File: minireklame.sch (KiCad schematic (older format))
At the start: 34 parts, among them IC1 ATXMEGA64A4U-A, P1 CONN_01X02, P10 CONN_01X04, P11 CONN_01X04, P12 CONN_01X04, P13 CONN_01X04, P14 CONN_01X04, P15 CONN_01X04, P16 CONN_01X04, P17 CONN_01X04, P2 CONN_01X04, P3 CONN_01X02, P3 CONN_01X04, P4 CONN_01X04, P5 CONN_01X04, P6 CONN_01X04, P7 CONN_01X04, P8 CONN_01X04, P9 CONN_01X04, U1 TLV1117-33CDCYR, U2 SP3483-EN-L, U3 TLC5955

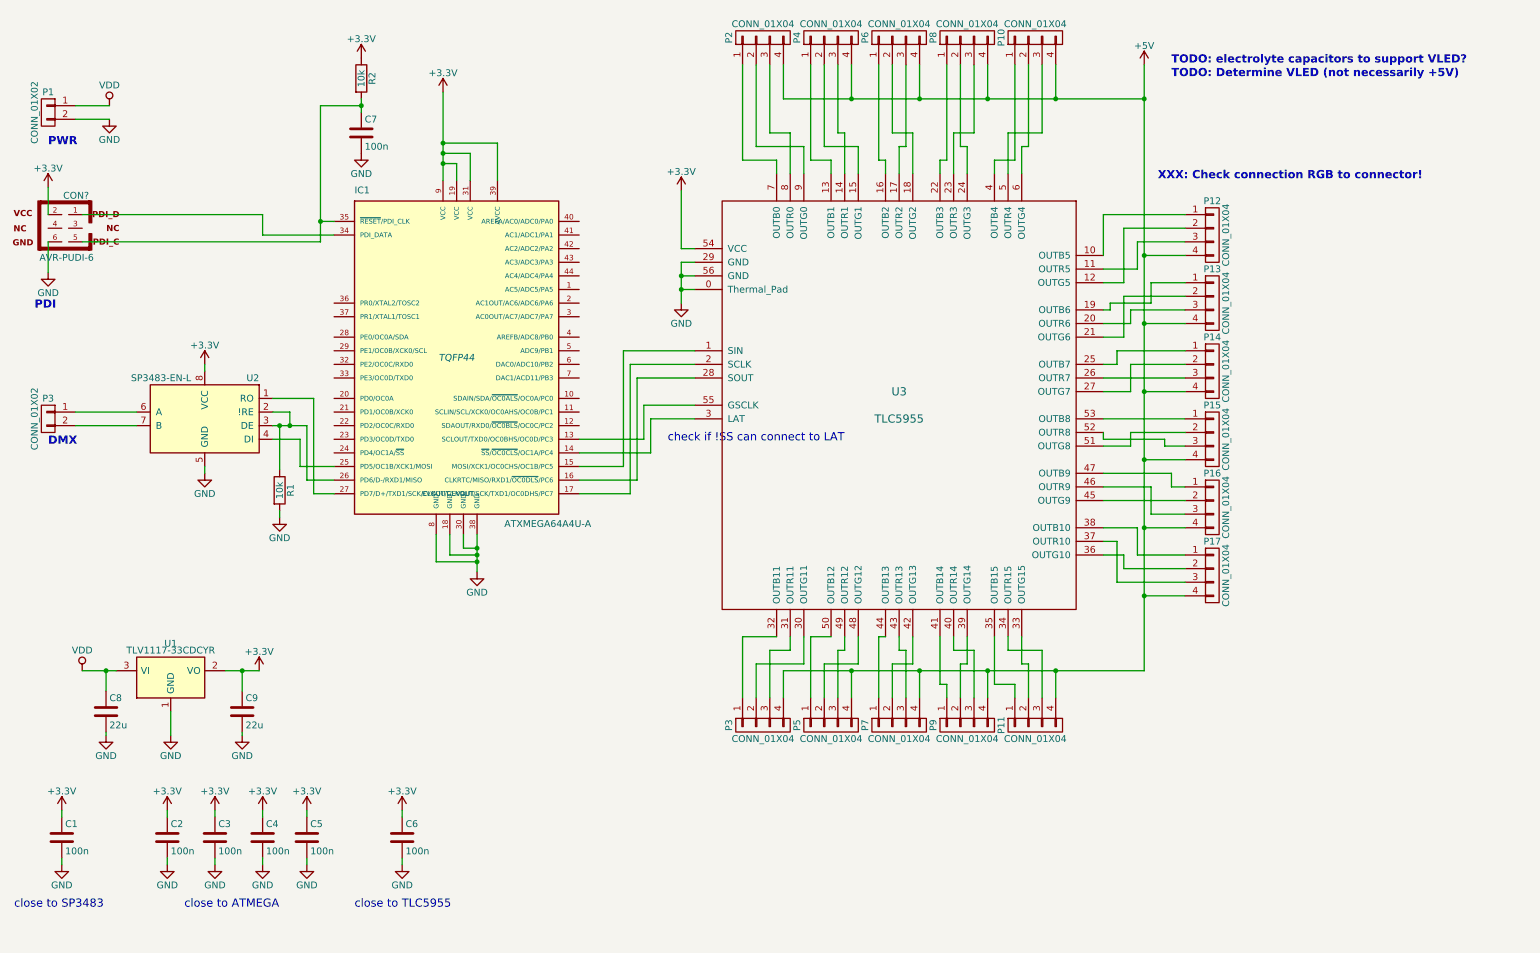
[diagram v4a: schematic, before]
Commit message: added optional XTAL
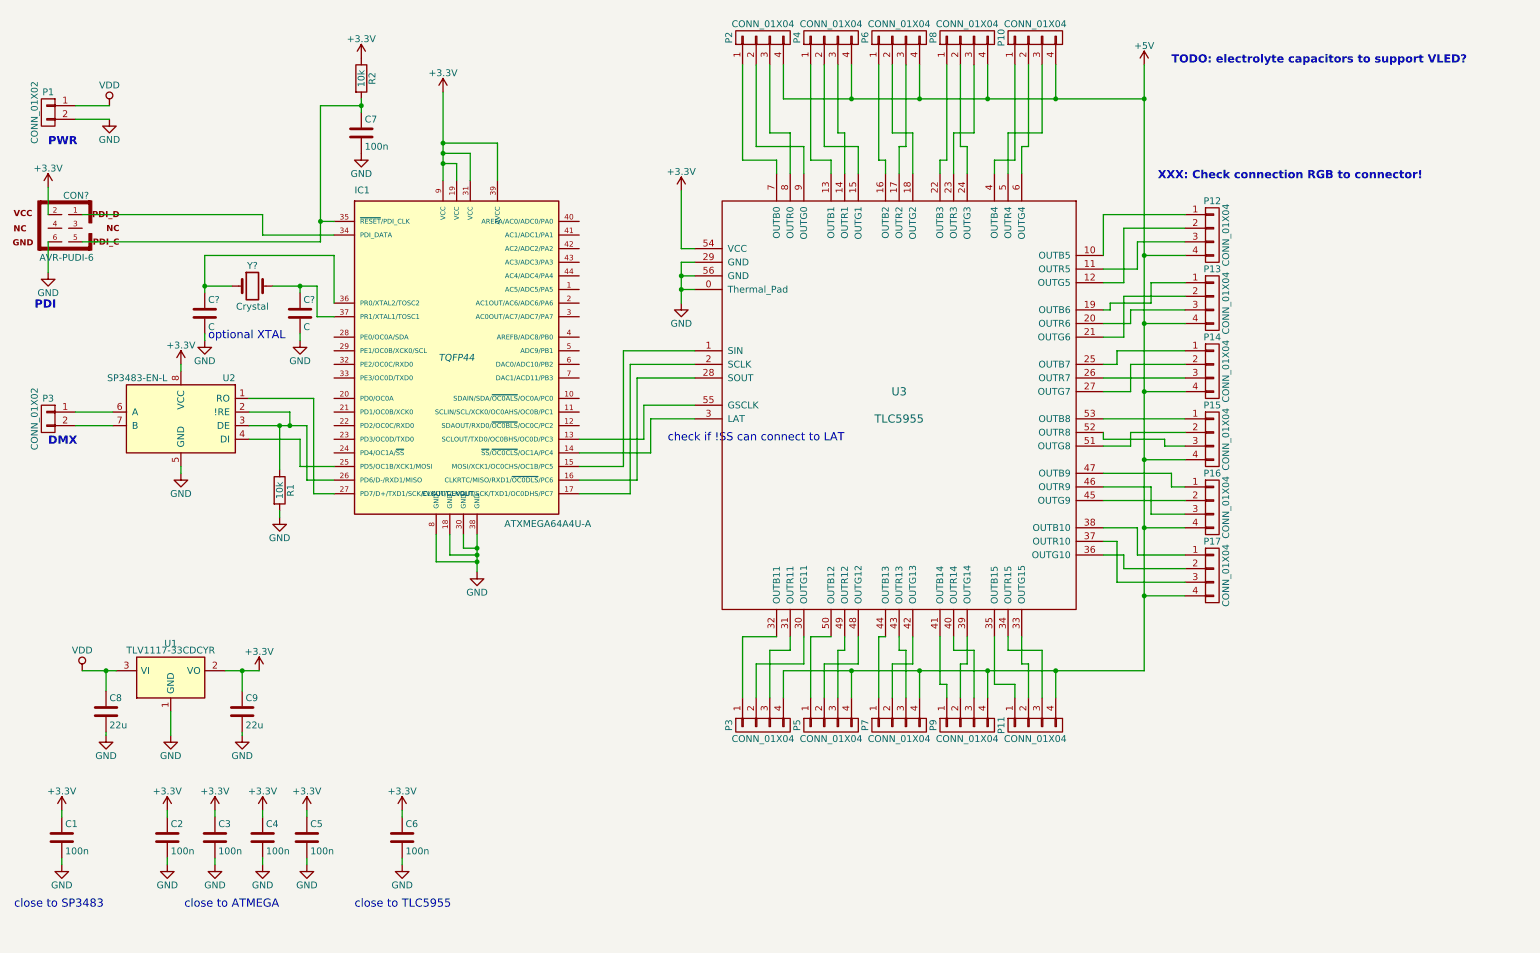
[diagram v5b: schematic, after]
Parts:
- added C? (x2): C, symbol C
- added Y?: Crystal, symbol Crystal
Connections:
- net GND: now also C?.2, C?.2
- net at IC1.36 (PR0/XTAL2/TOSC2): now also C?.1, Y?.1
- net at IC1.37 (PR1/XTAL1/TOSC1): now also C?.1, Y?.2
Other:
- note added: "optional XTAL"
- note removed: "TODO: Determine VLED (not necessarily +5V)"
- moved on the sheet: U2
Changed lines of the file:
@@
 L GND #PWR01
 U 1 1 58CAFE40
-P 2000 4150
-F 0 "#PWR01" H 2000 3900 50  0001 C CNN
-F 1 "GND" H 2000 4000 50  0000 C CNN
-F 2 "" H 2000 4150 50  0000 C CNN
-F 3 "" H 2000 4150 50  0000 C CNN
-	1    2000 4150
+P 1825 4150
+F 0 "#PWR01" H 1825 3900 50  0001 C CNN
+F 1 "GND" H 1825 4000 50  0000 C CNN
+F 2 "" H 1825 4150 50  0000 C CNN
+F 3 "" H 1825 4150 50  0000 C CNN
+	1    1825 4150
 	1    0    0    -1
 $EndComp
@@
 L SP3483-EN-L U2
 U 1 1 58CB0289
-P 2000 3750
-F 0 "U2" H 1600 4050 50  0000 L CNN
-F 1 "SP3483-EN-L" H 2100 4050 50  0000 L CNN
-F 2 "Housings_SOIC:SOIC-8_3.9x4.9mm_Pitch1.27mm" H 2000 3250 50  0001 C CIN
-F 3 "" H 2000 3750 50  0000 C CNN
-F 4 "SP3483EN-L" H 2000 3750 60  0001 C CNN "manf#"
-	1    2000 3750
+P 1825 3750
+F 0 "U2" H 1425 4050 50  0000 L CNN
+F 1 "SP3483-EN-L" H 1925 4050 50  0000 L CNN
+F 2 "Housings_SOIC:SOIC-8_3.9x4.9mm_Pitch1.27mm" H 1825 3250 50  0001 C CIN
+F 3 "" H 1825 3750 50  0000 C CNN
+F 4 "SP3483EN-L" H 1825 3750 60  0001 C CNN "manf#"
+	1    1825 3750
 	-1   0    0    -1
 $EndComp
@@
 L +3.3V #PWR02
 U 1 1 58CC36D0
-P 2000 3350
-F 0 "#PWR02" H 2000 3200 50  0001 C CNN
-F 1 "+3.3V" H 2000 3490 50  0000 C CNN
-F 2 "" H 2000 3350 50  0000 C CNN
-F 3 "" H 2000 3350 50  0000 C CNN
-	1    2000 3350
+P 1825 3350
+F 0 "#PWR02" H 1825 3200 50  0001 C CNN
+F 1 "+3.3V" H 1825 3490 50  0000 C CNN
+F 2 "" H 1825 3350 50  0000 C CNN
+F 3 "" H 1825 3350 50  0000 C CNN
+	1    1825 3350
 	1    0    0    -1
 $EndComp
@@
 $EndComp
 Wire Wire Line
-	1050 3700 1500 3700
-Wire Wire Line
-	1050 3800 1500 3800
-Wire Wire Line
-	2000 3350 2000 3400
+	1050 3700 1325 3700
+Wire Wire Line
+	1050 3800 1325 3800
+Wire Wire Line
+	1825 3350 1825 3400
 Wire Wire Line
 	3700 4600 3700 4800
@@
 	5500 2075 5500 2500
 Wire Wire Line
-	2500 3900 2700 3900
+	2325 3900 2700 3900
 Wire Wire Line
 	2700 3900 2700 4100
@@
 	2700 4100 2950 4100
 Wire Wire Line
-	2500 3800 2550 3800
+	2325 3800 2550 3800
 Wire Wire Line
 	2550 3800 2625 3800
@@
 	2750 4200 2950 4200
 Wire Wire Line
-	2500 3700 2625 3700
+	2325 3700 2625 3700
 Wire Wire Line
 	2625 3700 2625 3800
 Connection ~ 2625 3800
 Wire Wire Line
-	2500 3600 2800 3600
+	2325 3600 2800 3600
 Wire Wire Line
 	2800 3600 2800 4300
@@
 	1    0    0    -1
 $EndComp
-Text Notes 9100 1250 0    60   ~ 12
-TODO: Determine VLED (not necessarily +5V)
 $Comp
 L R R2
@@
 close to SP3483
 Wire Wire Line
-	2000 4150 2000 4100
+	1825 4150 1825 4100
 $Comp
 L +3.3V #PWR?
@@
 Text Notes 5400 3925 0    60   ~ 0
 check if !SS can connect to LAT
+$Comp
+L Crystal Y?
+U 1 1 591A9CF0
+P 2350 2775
+F 0 "Y?" H 2350 2925 50  0000 C CNN
+F 1 "Crystal" H 2350 2625 50  0000 C CNN
+F 2 "" H 2350 2775 50  0001 C CNN
+F 3 "" H 2350 2775 50  0001 C CNN
+	1    2350 2775
+	1    0    0    -1
+$EndComp
+Wire Wire Line
+	2950 2900 2950 2550
+Wire Wire Line
+	2950 2550 2000 2550
+Wire Wire Line
+	2000 2550 2000 2775
+Wire Wire Line
+	2000 2775 2000 2825
+Wire Wire Line
+	2000 2775 2200 2775
+Wire Wire Line
+	2950 3000 2825 3000
+Wire Wire Line
+	2825 3000 2825 2775
+Wire Wire Line
+	2825 2775 2700 2775
+Wire Wire Line
+	2700 2775 2500 2775
+$Comp
+L C C?
+U 1 1 591AA01D
+P 2000 2975
+F 0 "C?" H 2025 3075 50  0000 L CNN
+F 1 "C" H 2025 2875 50  0000 L CNN
+F 2 "" H 2038 2825 50  0001 C CNN
+F 3 "" H 2000 2975 50  0001 C CNN
+	1    2000 2975
+	1    0    0    -1
+$EndComp
+$Comp
+L C C?
+U 1 1 591AA0D4
+P 2700 2975
+F 0 "C?" H 2725 3075 50  0000 L CNN
+F 1 "C" H 2725 2875 50  0000 L CNN
+F 2 "" H 2738 2825 50  0001 C CNN
+F 3 "" H 2700 2975 50  0001 C CNN
+	1    2700 2975
+	1    0    0    -1
+$EndComp
+$Comp
+L GND #PWR?
+U 1 1 591AA144
+P 2700 3175
+F 0 "#PWR?" H 2700 2925 50  0001 C CNN
+F 1 "GND" H 2700 3025 50  0000 C CNN
+F 2 "" H 2700 3175 50  0001 C CNN
+F 3 "" H 2700 3175 50  0001 C CNN
+	1    2700 3175
+	1    0    0    -1
+$EndComp
+$Comp
+L GND #PWR?
+U 1 1 591AA32F
+P 2000 3175
+F 0 "#PWR?" H 2000 2925 50  0001 C CNN
+F 1 "GND" H 2000 3025 50  0000 C CNN
+F 2 "" H 2000 3175 50  0001 C CNN
+F 3 "" H 2000 3175 50  0001 C CNN
+	1    2000 3175
+	1    0    0    -1
+$EndComp
+Wire Wire Line
+	2000 3125 2000 3175
+Wire Wire Line
+	2700 3175 2700 3125
+Wire Wire Line
+	2700 2825 2700 2775
+Connection ~ 2700 2775
+Connection ~ 2000 2775
+Text Notes 2025 3175 0    60   ~ 0
+optional XTAL
 $EndSCHEMATC

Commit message: DMX now with in and out
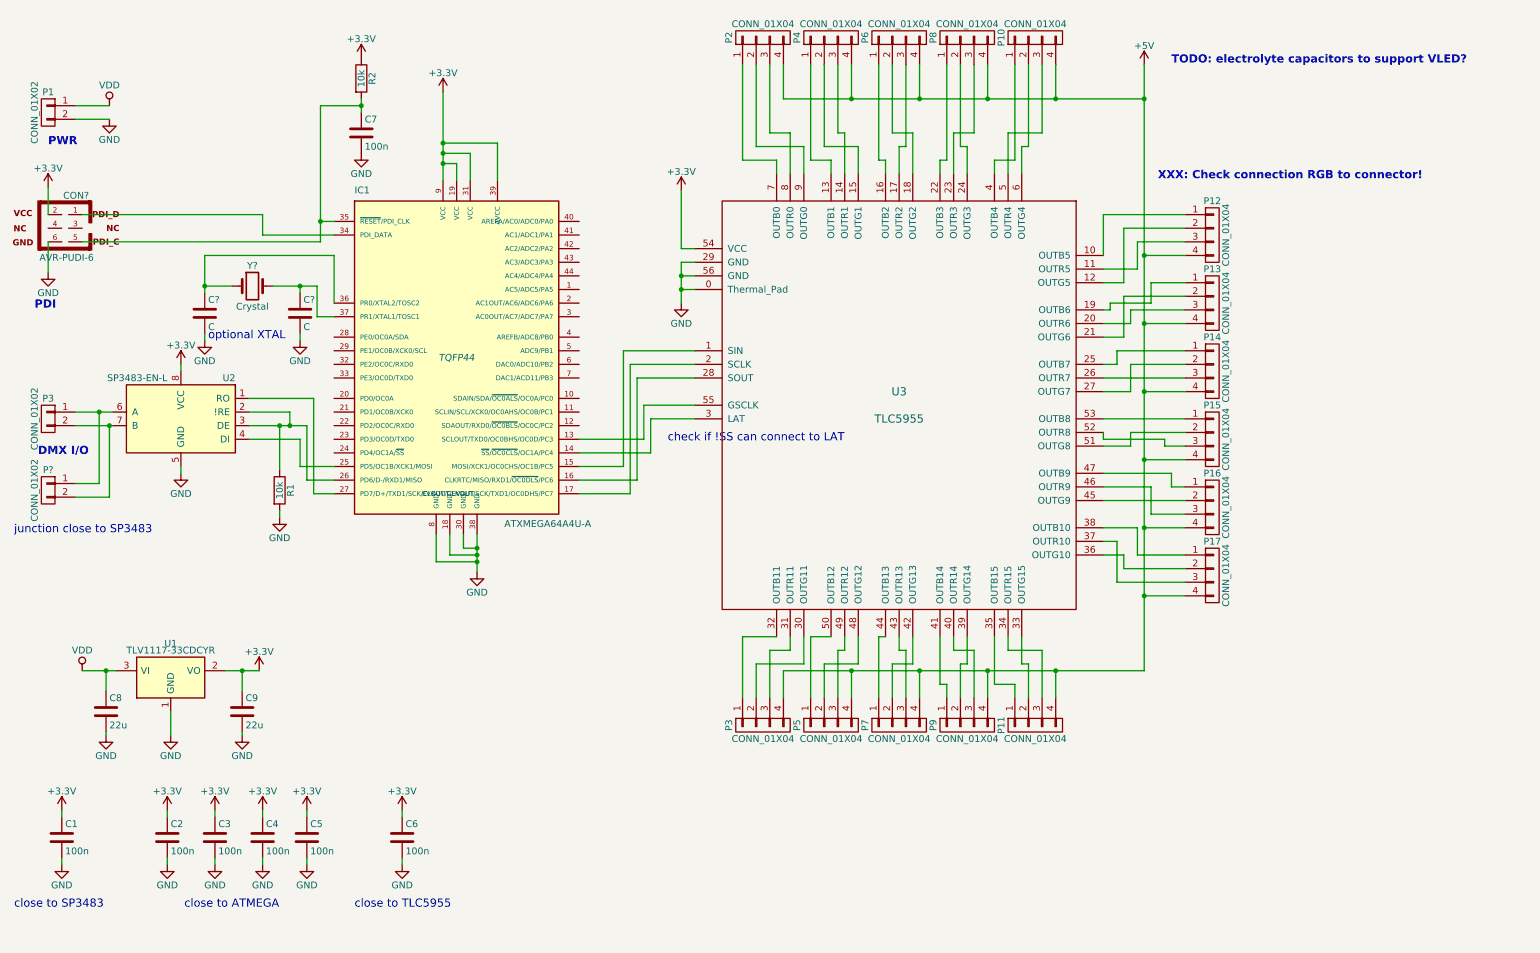
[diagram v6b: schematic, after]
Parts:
- added P?: CONN_01X02, symbol CONN_01X02
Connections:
- net at P3.1 (P1), U2.6 (A): now also P?.1 (P1)
- net at P3.2 (P2), U2.7 (B): now also P?.2 (P2)
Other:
- note added: "DMX I/O"
- note added: "junction close to SP3483"
- note removed: "DMX"
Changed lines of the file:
@@
 	3700 4600 3700 4800
 Wire Wire Line
-	4000 4600 4000 4700
-Wire Wire Line
-	4000 4700 4000 4750
-Wire Wire Line
-	4000 4750 4000 4800
-Wire Wire Line
-	4000 4800 4000 4875
+	4000 4600 4000 4875
 Wire Wire Line
 	3900 4600 3900 4700
@@
 	5500 2800 5600 2800
 Wire Wire Line
-	5500 2600 5500 2700
-Wire Wire Line
-	5500 2700 5500 2800
-Wire Wire Line
-	5500 2800 5500 2900
+	5500 2600 5500 2900
 Wire Wire Line
 	5600 2700 5500 2700
@@
 Connection ~ 5500 2700
 Wire Wire Line
-	3750 1350 3750 1725
-Wire Wire Line
-	3750 1725 3750 1800
-Wire Wire Line
-	3750 1800 3750 1875
-Wire Wire Line
-	3750 1875 3750 2000
+	3750 1350 3750 2000
 Wire Wire Line
 	5500 2500 5600 2500
@@
 	2700 4100 2950 4100
 Wire Wire Line
-	2325 3800 2550 3800
-Wire Wire Line
-	2550 3800 2625 3800
-Wire Wire Line
-	2625 3800 2750 3800
+	2325 3800 2750 3800
 Wire Wire Line
 	2750 3800 2750 4200
@@
 	6250 1150 6250 1400
 Wire Wire Line
-	6250 1400 6750 1400
-Wire Wire Line
-	6750 1400 7250 1400
-Wire Wire Line
-	7250 1400 7750 1400
-Wire Wire Line
-	7750 1400 8250 1400
-Wire Wire Line
-	8250 1400 8900 1400
-Wire Wire Line
-	8900 5600 8900 5050
-Wire Wire Line
-	8900 5050 8900 4550
-Wire Wire Line
-	8900 4550 8900 4050
-Wire Wire Line
-	8900 4050 8900 3550
-Wire Wire Line
-	8900 3550 8900 3050
-Wire Wire Line
-	8900 3050 8900 2550
-Wire Wire Line
-	8900 2550 8900 1400
-Wire Wire Line
-	8900 1400 8900 1150
+	6250 1400 8900 1400
+Wire Wire Line
+	8900 5600 8900 1150
 Wire Wire Line
 	6750 1150 6750 1400
@@
 	6250 5800 6250 5600
 Wire Wire Line
-	6250 5600 6750 5600
-Wire Wire Line
-	6750 5600 7250 5600
-Wire Wire Line
-	7250 5600 7750 5600
-Wire Wire Line
-	7750 5600 8250 5600
-Wire Wire Line
-	8250 5600 8900 5600
+	6250 5600 8900 5600
 Connection ~ 8900 5050
 Wire Wire Line
@@
 $EndComp
 Wire Wire Line
-	1100 5600 1275 5600
-Wire Wire Line
-	1275 5600 1350 5600
+	1100 5600 1350 5600
 $Comp
 L GND #PWR012
@@
 	2850 1450 3150 1450
 Wire Wire Line
-	3150 1400 3150 1450
-Wire Wire Line
-	3150 1450 3150 1500
+	3150 1400 3150 1500
 Connection ~ 3150 1450
 $Comp
@@
 	1050 1550 1300 1550
 Wire Wire Line
-	2850 1450 2850 2300
-Wire Wire Line
-	2850 2300 2850 2450
+	2850 1450 2850 2450
 Text Notes 850  1750 0    60   ~ 12
 PWR
 Text Notes 750  2950 0    60   ~ 12
 PDI
-Text Notes 850  3950 0    60   ~ 12
-DMX
+Text Notes 775  4025 0    60   ~ 12
+DMX I/O
 $Comp
 L AVR-PUDI-6 CON?
@@
 	1750 5900 1750 6075
 Wire Wire Line
-	2150 5600 2275 5600
-Wire Wire Line
-	2275 5600 2400 5600
+	2150 5600 2400 5600
 Wire Wire Line
 	2275 5750 2275 5600
@@
 	2950 2550 2000 2550
 Wire Wire Line
-	2000 2550 2000 2775
-Wire Wire Line
-	2000 2775 2000 2825
+	2000 2550 2000 2825
 Wire Wire Line
 	2000 2775 2200 2775
@@
 	2825 3000 2825 2775
 Wire Wire Line
-	2825 2775 2700 2775
-Wire Wire Line
-	2700 2775 2500 2775
+	2825 2775 2500 2775
 $Comp
 L C C?
@@
 Text Notes 2025 3175 0    60   ~ 0
 optional XTAL
+$Comp
+L CONN_01X02 P?
+U 1 1 591AAFD2
+P 850 4275
+F 0 "P?" H 850 4425 50  0000 C CNN
+F 1 "CONN_01X02" V 950 4275 50  0000 C CNN
+F 2 "" H 850 4275 50  0000 C CNN
+F 3 "" H 850 4275 50  0000 C CNN
+	1    850  4275
+	-1   0    0    -1
+$EndComp
+Wire Wire Line
+	1050 4325 1300 4325
+Wire Wire Line
+	1300 4325 1300 3800
+Connection ~ 1300 3800
+Wire Wire Line
+	1050 4225 1225 4225
+Wire Wire Line
+	1225 4225 1225 3700
+Connection ~ 1225 3700
+Text Notes 600  4600 0    60   ~ 0
+junction close to SP3483
 $EndSCHEMATC
